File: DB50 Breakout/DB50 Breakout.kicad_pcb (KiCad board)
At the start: 2 copper layers, 100 x 100 mm, 8 parts, among them P1 CONN_02X25, P2 CONN_01X02, P3 CONN_01X06, P4 CONN_01X06, P5 CONN_01X06, P6 CONN_01X06, P7 CONN_01X06, P8 CONN_01X06

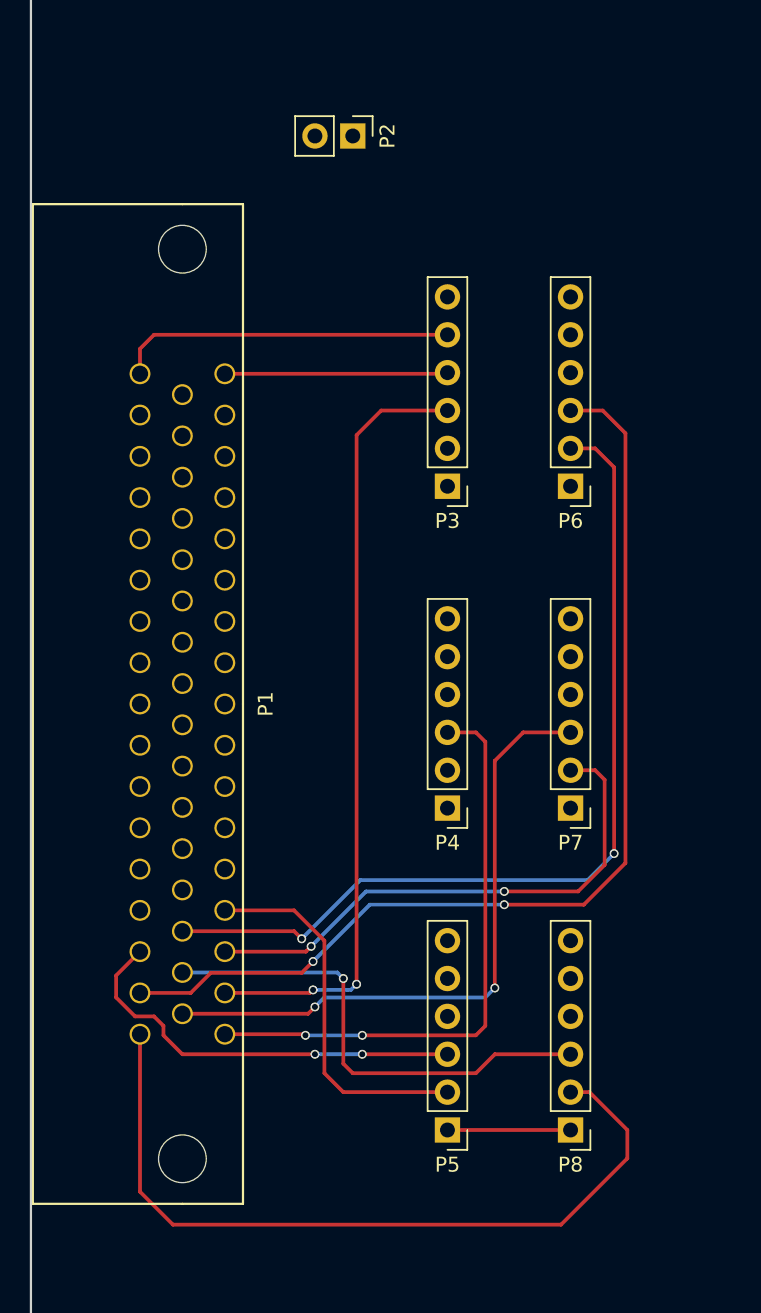
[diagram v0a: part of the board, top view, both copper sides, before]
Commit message: Updated DB50 breakout
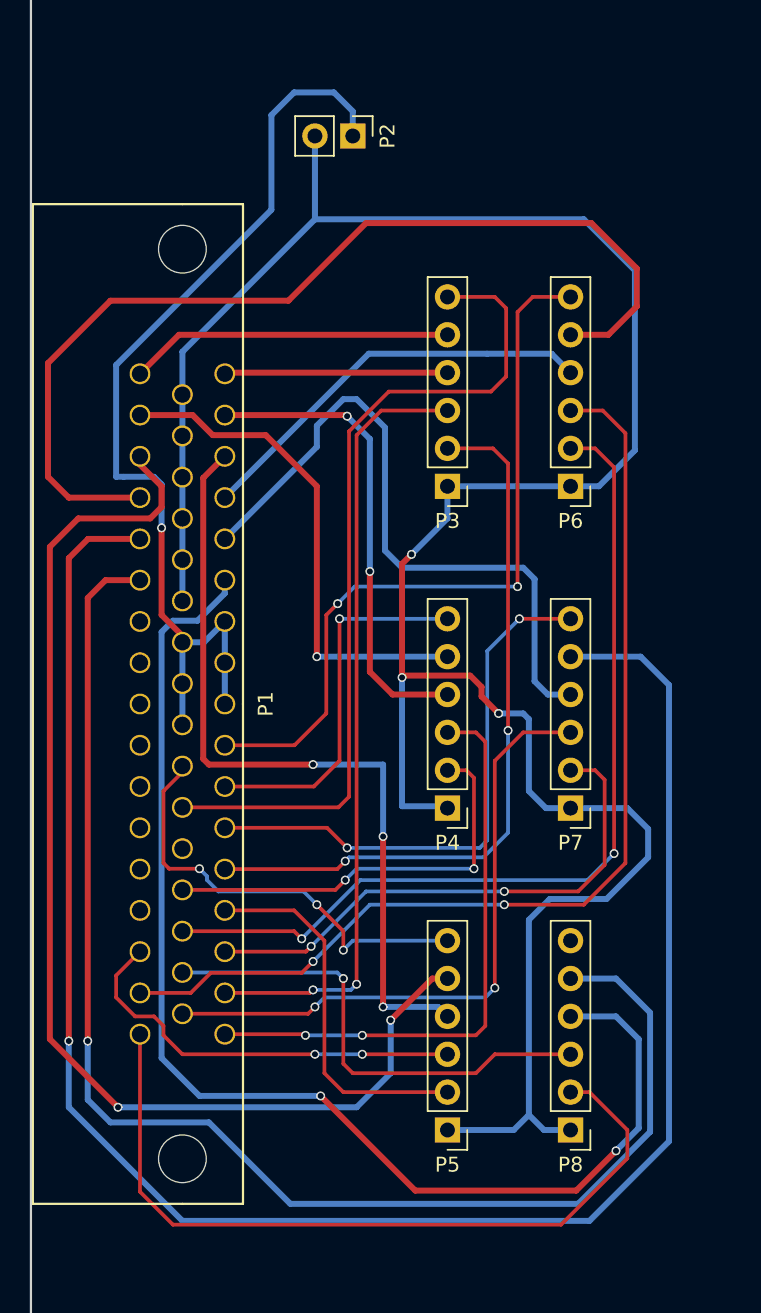
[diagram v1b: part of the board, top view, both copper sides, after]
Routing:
- net GND: track 8.25 -> 180.9 mm, vias 0 -> 3
- net M4_2: track 0.00 -> 125.8 mm, vias 0 -> 1
- net M5_2: track 0.00 -> 94.5 mm, vias 0 -> 1
- net M5_1: track 0.00 -> 83.4 mm, vias 0 -> 2
- net M2_2: track 0.00 -> 79.8 mm, vias 0 -> 2
- net LED_VCC: track 0.00 -> 78.8 mm, vias 0 -> 1
- net M3_2: track 0.00 -> 66.8 mm
- net Rot_limit: track 0.00 -> 56.9 mm
- net M2_1: track 0.00 -> 54.0 mm, vias 0 -> 3
- net Limit_3: track 0.00 -> 50.3 mm, vias 0 -> 2
- net ROT_1: track 0.00 -> 49.3 mm, vias 0 -> 2
- net M4_1: track 0.00 -> 45.0 mm
- net Limit_4: track 0.00 -> 37.6 mm, vias 0 -> 2
- net M1_2: track 0.00 -> 34.0 mm, vias 0 -> 1
- net M1_1: track 0.00 -> 31.9 mm, vias 0 -> 2
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
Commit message: Updated DB50 breakout size
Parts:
- added REF**: MountingHole_3.2mm_M3, MountingHole:MountingHole_3.2mm_M3, F.Cu at (74.9, 133.5)
- added REF**: MountingHole_3.2mm_M3, MountingHole:MountingHole_3.2mm_M3, F.Cu at (135.1, 133.3)
- added REF**: MountingHole_3.2mm_M3, MountingHole:MountingHole_3.2mm_M3, F.Cu at (134.9, 57.1)
- added REF**: MountingHole_3.2mm_M3, MountingHole:MountingHole_3.2mm_M3, F.Cu at (75.4, 57.4)
- added REF**: PinHeader_2x20_P2.54mm_Vertical, Connector_PinHeader_2.54mm:PinHeader_2x20_P2.54mm_Vertical, F.Cu at (119.1, 70.9)
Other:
- board size 100 x 100 mm -> 67.8 x 84.2 mm

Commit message: Updated breakout
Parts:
- added REF**: PinHeader_2x20_P2.54mm_Vertical, Connector_PinHeader_2.54mm:PinHeader_2x20_P2.54mm_Vertical, F.Cu at (132.3, 70.9)
- added REF**: PinHeader_2x20_P2.54mm_Vertical, Connector_PinHeader_2.54mm:PinHeader_2x20_P2.54mm_Vertical, F.Cu at (127.3, 70.9)
- added REF**: PinHeader_2x20_P2.54mm_Vertical, Connector_PinHeader_2.54mm:PinHeader_2x20_P2.54mm_Vertical, F.Cu at (122.2, 70.9)
- moved REF** 2.03 mm to (117.1, 70.9)
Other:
- board text added: "Axis 1"
- board text added: "Axis 2"
- board text added: "Axis 3"
- board text added: "Axis 4"
- board text added: "Axis 5"
- board text added: "GND"
- board text added: "LED VCC"
- board text added: "Limit Encoder 2 Encoder 1 Motor 2 Motor 1 GND"
- board text added: "Rotary axis"
- board text added: "Scorebot ER3 DB50 breakout V1.0 By Ethan"
- board text added: "https://github.com/ethanleep/robotic-arm"
